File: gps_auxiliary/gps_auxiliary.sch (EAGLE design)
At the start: 3 parts, among them J1 FAN, J2 EHT-110-01-S-D, U1 PYB10-Q24-S3

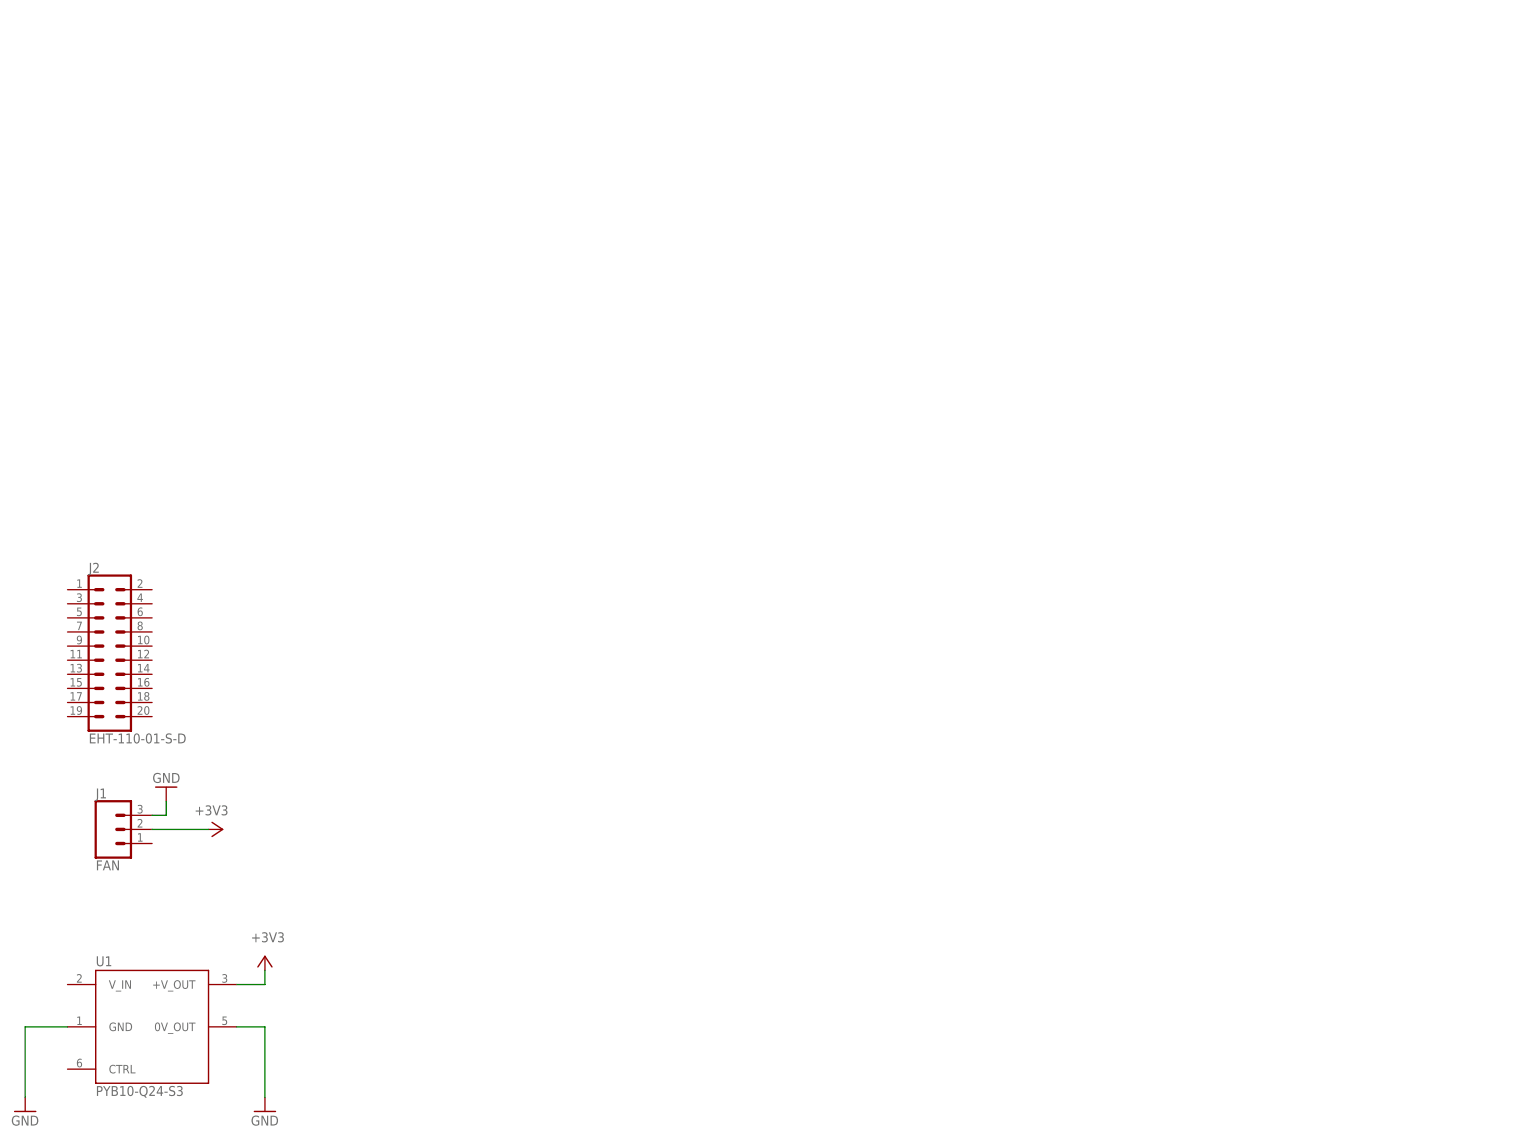
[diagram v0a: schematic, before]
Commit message: Added 6x2 connector, finished schematic
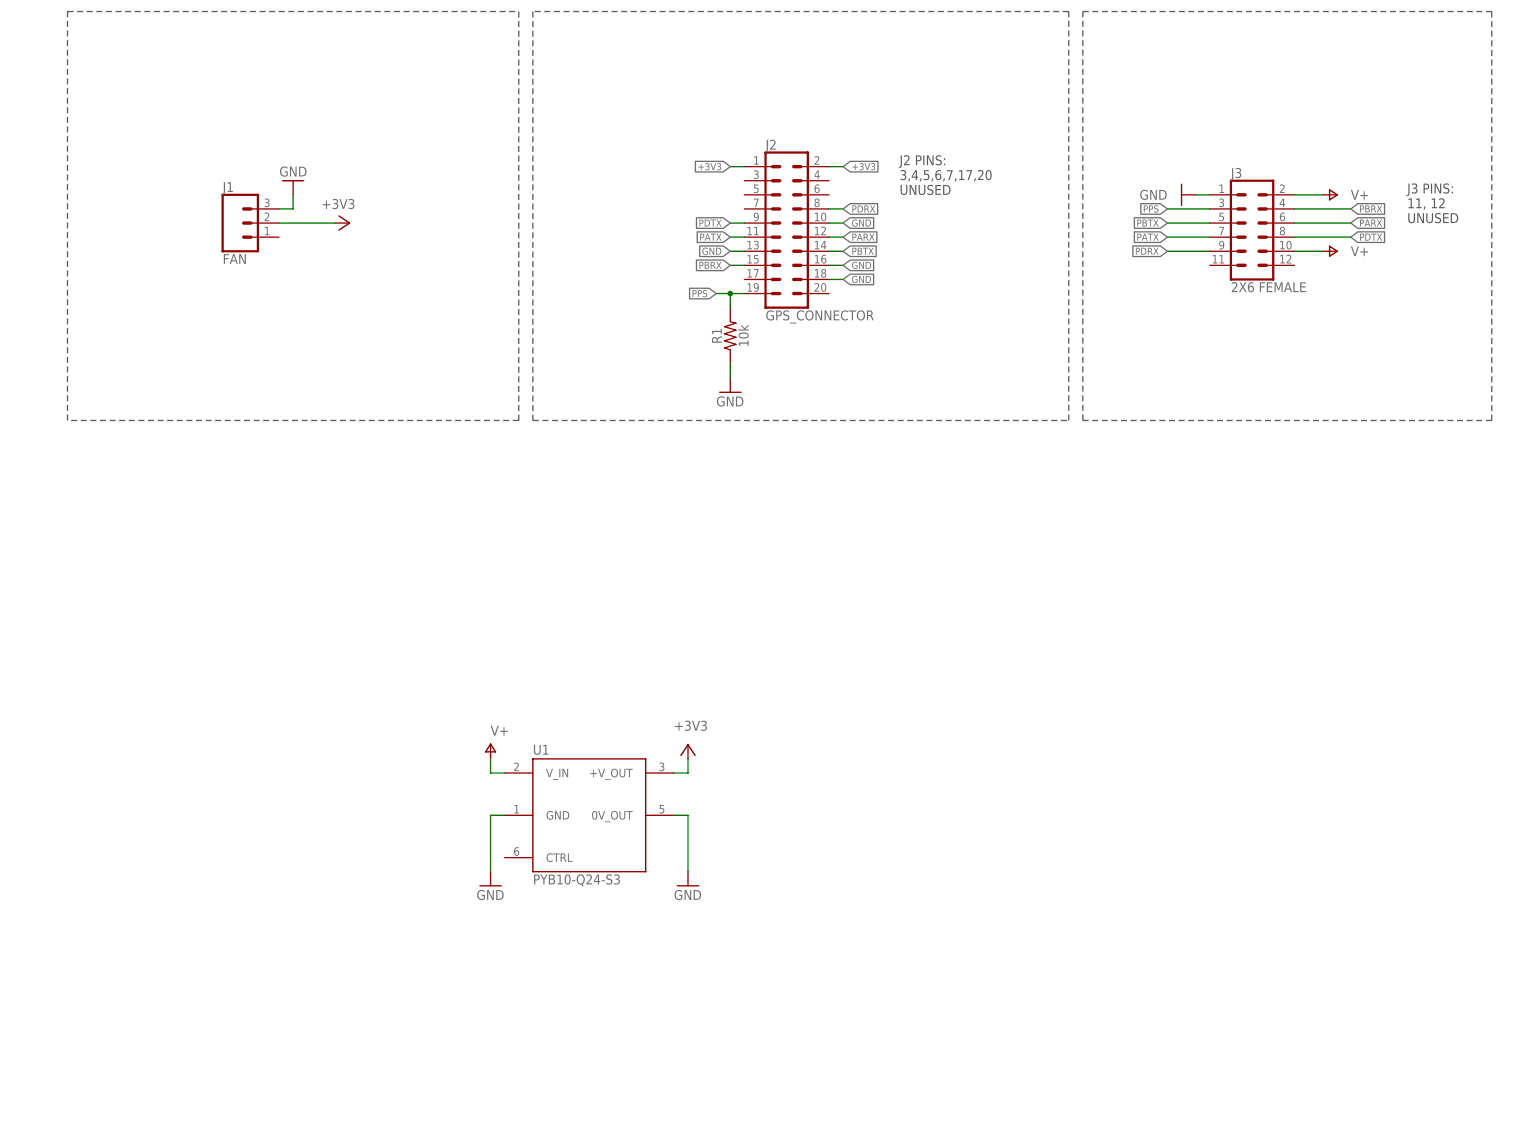
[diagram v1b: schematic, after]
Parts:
- added J3: 2X6 FEMALE, gps_auxiliary:CONN_06X2PTH_FEMALE
- added R1: 10k, gps_auxiliary:CFR-25JB-52-10K
- J2: value EHT-110-01-S-D -> GPS_CONNECTOR
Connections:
- new net PARX: J2.12, J3.6
- new net PATX: J2.11, J3.7
- new net PBRX: J2.15, J3.4
- new net PBTX: J2.14, J3.5
- new net PDRX: J2.8, J3.9
- new net PDTX: J2.9, J3.8
- new net PPS: J2.19, J3.3, R1.2
- new net V+: J3.10, J3.2, U1.V_IN
- net +3V3: now also J2.1, J2.2
- net GND: now also J2.10, J2.13, J2.16, J2.18, J3.1, R1.1
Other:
- note added: "J2 PINS: 3,4,5,6,7,17,20 UNUSED"
- note added: "J3 PINS: 11, 12 UNUSED"
- moved on the sheet: J1, J2, U1

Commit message: Finished GPS board design
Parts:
- J2: value GPS_CONNECTOR -> GPS
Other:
- note added: "COMPUTE CONN"
- note added: "FAN CONN"
- note added: "GPS CONN"
- note added: "VOLTAGE REG"
- moved on the sheet: U1
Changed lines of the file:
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@@
 <parts>
 <part name="J1" library="gps_auxiliary" deviceset="ED700/3" device="" value="FAN"/>
-<part name="J2" library="gps_auxiliary" deviceset="EHT-110-01-S-D" device="" value="GPS_CONNECTOR"/>
+<part name="J2" library="gps_auxiliary" deviceset="EHT-110-01-S-D" device="" value="GPS"/>
 <part name="U1" library="gps_auxiliary" deviceset="PYB10-Q24-S3" device=""/>
 <part name="+3V1" library="supply1" library_urn="urn:adsk.eagle:library:371" deviceset="+3V3" device=""/>
@@
 <wire x1="269.24" y1="132.08" x2="195.58" y2="132.08" width="0.1524" layer="97" style="shortdash"/>
 <wire x1="195.58" y1="132.08" x2="195.58" y2="205.74" width="0.1524" layer="97" style="shortdash"/>
+<wire x1="93.98" y1="129.54" x2="12.7" y2="129.54" width="0.1524" layer="97" style="shortdash"/>
+<wire x1="12.7" y1="129.54" x2="12.7" y2="45.72" width="0.1524" layer="97" style="shortdash"/>
+<wire x1="93.98" y1="129.54" x2="93.98" y2="45.72" width="0.1524" layer="97" style="shortdash"/>
+<wire x1="93.98" y1="45.72" x2="12.7" y2="45.72" width="0.1524" layer="97" style="shortdash"/>
+<text x="15.24" y="195.58" size="6.4516" layer="97" font="vector" ratio="12">FAN CONN</text>
+<text x="99.06" y="195.58" size="6.4516" layer="97" font="vector" ratio="12">GPS CONN</text>
+<text x="198.12" y="195.58" size="6.4516" layer="97" font="vector" ratio="12">COMPUTE CONN</text>
+<text x="15.24" y="119.38" size="6.4516" layer="97" font="vector" ratio="12">VOLTAGE REG</text>
 </plain>
 <instances>
@@
 <attribute name="NAME" x="138.43" y="180.848" size="1.778" layer="95" font="vector"/>
 </instance>
-<instance part="U1" gate="G$1" x="106.68" y="60.96" smashed="yes">
-<attribute name="NAME" x="96.52" y="71.882" size="1.778" layer="95" font="vector"/>
-<attribute name="VALUE" x="96.52" y="48.514" size="1.778" layer="96" font="vector"/>
+<instance part="U1" gate="G$1" x="53.34" y="83.82" smashed="yes">
+<attribute name="NAME" x="43.18" y="94.742" size="1.778" layer="95" font="vector"/>
+<attribute name="VALUE" x="43.18" y="71.374" size="1.778" layer="96" font="vector"/>
 </instance>
 <instance part="+3V1" gate="G$1" x="63.5" y="167.64" smashed="yes" rot="R270">
@@
 <attribute name="VALUE" x="55.88" y="177.8" size="1.778" layer="96" rot="R180"/>
 </instance>
-<instance part="+3V2" gate="G$1" x="124.46" y="73.66" smashed="yes">
-<attribute name="VALUE" x="121.92" y="76.2" size="1.778" layer="96"/>
-</instance>
-<instance part="GND2" gate="1" x="88.9" y="48.26" smashed="yes">
-<attribute name="VALUE" x="86.36" y="45.72" size="1.778" layer="96"/>
-</instance>
-<instance part="GND3" gate="1" x="124.46" y="48.26" smashed="yes">
-<attribute name="VALUE" x="121.92" y="45.72" size="1.778" layer="96"/>
+<instance part="+3V2" gate="G$1" x="71.12" y="96.52" smashed="yes">
+<attribute name="VALUE" x="68.58" y="99.06" size="1.778" layer="96"/>
+</instance>
+<instance part="GND2" gate="1" x="35.56" y="71.12" smashed="yes">
+<attribute name="VALUE" x="33.02" y="68.58" size="1.778" layer="96"/>
+</instance>
+<instance part="GND3" gate="1" x="71.12" y="71.12" smashed="yes">
+<attribute name="VALUE" x="68.58" y="68.58" size="1.778" layer="96"/>
 </instance>
 <instance part="J3" gate="G$1" x="226.06" y="167.64" smashed="yes">
@@
 <attribute name="VALUE" x="243.84" y="162.56" size="1.778" layer="96" align="center-left"/>
 </instance>
-<instance part="P+3" gate="1" x="88.9" y="73.66" smashed="yes">
-<attribute name="VALUE" x="88.9" y="76.2" size="1.778" layer="96" align="center-left"/>
+<instance part="P+3" gate="1" x="35.56" y="96.52" smashed="yes">
+<attribute name="VALUE" x="35.56" y="99.06" size="1.778" layer="96" align="center-left"/>
 </instance>
 <instance part="FRAME1" gate="G$1" x="0" y="0" smashed="yes"/>
@@
 <segment>
 <pinref part="U1" gate="G$1" pin="+V_OUT"/>
-<wire x1="121.92" y1="68.58" x2="124.46" y2="68.58" width="0.1524" layer="91"/>
-<wire x1="124.46" y1="68.58" x2="124.46" y2="71.12" width="0.1524" layer="91"/>
+<wire x1="68.58" y1="91.44" x2="71.12" y2="91.44" width="0.1524" layer="91"/>
+<wire x1="71.12" y1="91.44" x2="71.12" y2="93.98" width="0.1524" layer="91"/>
 <pinref part="+3V2" gate="G$1" pin="+3V3"/>
 </segment>
@@
 <segment>
 <pinref part="U1" gate="G$1" pin="GND"/>
-<wire x1="91.44" y1="60.96" x2="88.9" y2="60.96" width="0.1524" layer="91"/>
-<wire x1="88.9" y1="60.96" x2="88.9" y2="50.8" width="0.1524" layer="91"/>
+<wire x1="38.1" y1="83.82" x2="35.56" y2="83.82" width="0.1524" layer="91"/>
+<wire x1="35.56" y1="83.82" x2="35.56" y2="73.66" width="0.1524" layer="91"/>
 <pinref part="GND2" gate="1" pin="GND"/>
 </segment>
 <segment>
 <pinref part="U1" gate="G$1" pin="0V_OUT"/>
-<wire x1="121.92" y1="60.96" x2="124.46" y2="60.96" width="0.1524" layer="91"/>
-<wire x1="124.46" y1="60.96" x2="124.46" y2="50.8" width="0.1524" layer="91"/>
+<wire x1="68.58" y1="83.82" x2="71.12" y2="83.82" width="0.1524" layer="91"/>
+<wire x1="71.12" y1="83.82" x2="71.12" y2="73.66" width="0.1524" layer="91"/>
 <pinref part="GND3" gate="1" pin="GND"/>
 </segment>
@@
 <segment>
 <pinref part="U1" gate="G$1" pin="V_IN"/>
-<wire x1="91.44" y1="68.58" x2="88.9" y2="68.58" width="0.1524" layer="91"/>
-<wire x1="88.9" y1="68.58" x2="88.9" y2="71.12" width="0.1524" layer="91"/>
+<wire x1="38.1" y1="91.44" x2="35.56" y2="91.44" width="0.1524" layer="91"/>
+<wire x1="35.56" y1="91.44" x2="35.56" y2="93.98" width="0.1524" layer="91"/>
 <pinref part="P+3" gate="1" pin="V+"/>
 </segment>

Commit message: Added capacitor to library and board
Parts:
- added C1, C2: 10uF 50V, gps_auxiliary:CAP-5MM
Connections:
- net +3V3: now also C2.1
- net GND: now also C1.2, C2.2
- net V+: now also C1.1
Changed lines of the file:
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@@
 <part name="P+3" library="supply1" library_urn="urn:adsk.eagle:library:371" deviceset="V+" device=""/>
 <part name="FRAME1" library="frames" library_urn="urn:adsk.eagle:library:229" deviceset="FRAME_A_L" device=""/>
+<part name="C1" library="gps_auxiliary" deviceset="CAP-5MM" device="" value="10uF 50V"/>
+<part name="C2" library="gps_auxiliary" deviceset="CAP-5MM" device="" value="10uF 50V"/>
 </parts>
 <sheets>
@@
 <attribute name="DRAWING_NAME" x="190.5" y="19.05" size="2.54" layer="94"/>
 </instance>
+<instance part="C1" gate="G$1" x="35.56" y="86.36" smashed="yes">
+<attribute name="NAME" x="34.544" y="89.281" size="1.778" layer="95" font="vector" align="bottom-right"/>
+<attribute name="VALUE" x="34.544" y="84.201" size="1.778" layer="96" font="vector" align="bottom-right"/>
+</instance>
+<instance part="C2" gate="G$1" x="71.12" y="86.36" smashed="yes">
+<attribute name="NAME" x="72.644" y="89.281" size="1.778" layer="95" font="vector"/>
+<attribute name="VALUE" x="72.644" y="84.201" size="1.778" layer="96" font="vector"/>
+</instance>
 </instances>
 <busses>
@@
 <wire x1="71.12" y1="91.44" x2="71.12" y2="93.98" width="0.1524" layer="91"/>
 <pinref part="+3V2" gate="G$1" pin="+3V3"/>
+<pinref part="C2" gate="G$1" pin="1"/>
+<junction x="71.12" y="91.44"/>
 </segment>
 <segment>
@@
 <wire x1="35.56" y1="83.82" x2="35.56" y2="73.66" width="0.1524" layer="91"/>
 <pinref part="GND2" gate="1" pin="GND"/>
+<pinref part="C1" gate="G$1" pin="2"/>
+<junction x="35.56" y="83.82"/>
 </segment>
 <segment>
@@
 <wire x1="71.12" y1="83.82" x2="71.12" y2="73.66" width="0.1524" layer="91"/>
 <pinref part="GND3" gate="1" pin="GND"/>
+<pinref part="C2" gate="G$1" pin="2"/>
+<junction x="71.12" y="83.82"/>
 </segment>
 <segment>
@@
 <wire x1="35.56" y1="91.44" x2="35.56" y2="93.98" width="0.1524" layer="91"/>
 <pinref part="P+3" gate="1" pin="V+"/>
-</segment>
-</net>
+<pinref part="C1" gate="G$1" pin="1"/>
+<junction x="35.56" y="91.44"/>
+</segment>
+</net>
